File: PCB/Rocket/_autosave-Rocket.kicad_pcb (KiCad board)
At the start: 2 copper layers, 62.7 x 63.5 mm, 49 parts, among them J4 Micro_SD_Card, J5 Conn_ARM_JTAG_SWD_10, J7 1987724, U1 STM32L476RGTx, U2 MIC5365-3.3YC5-TR, U3 MC78L05ACDR2G

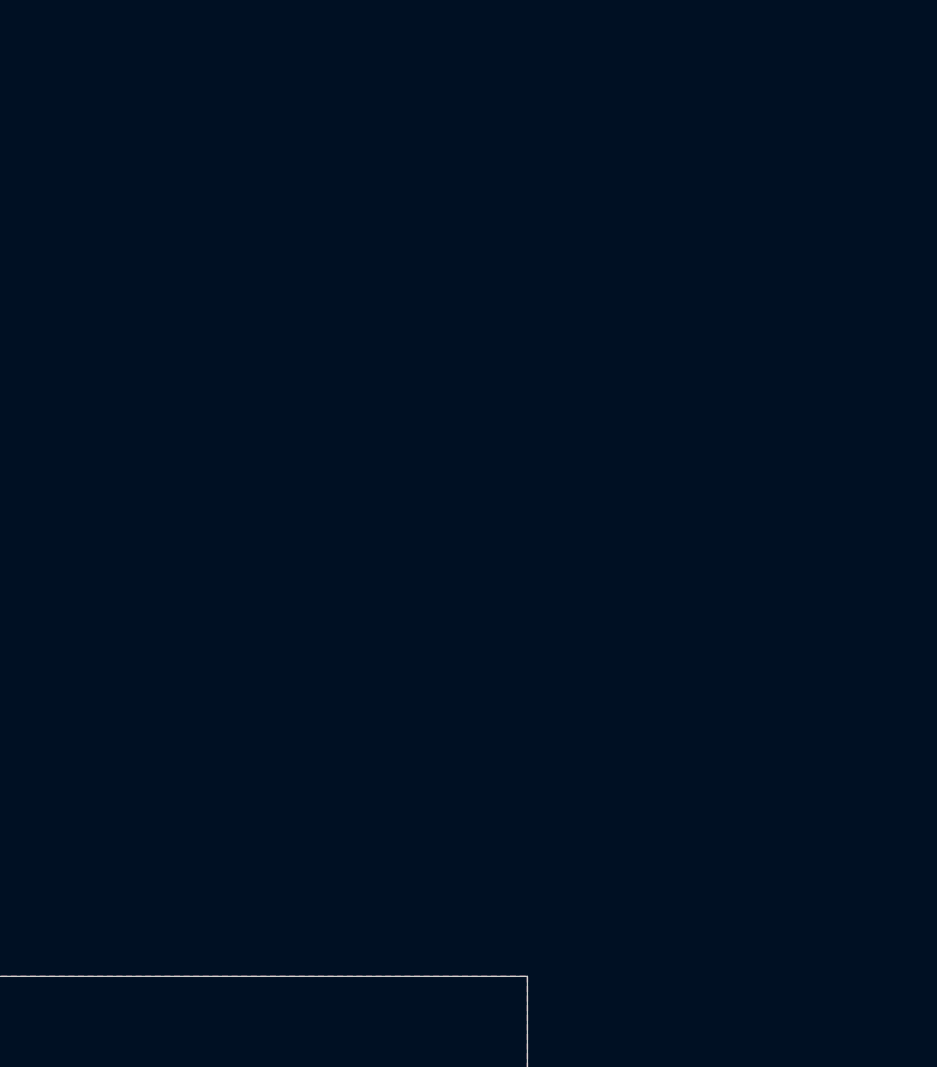
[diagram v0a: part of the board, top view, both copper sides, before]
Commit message: Updating to use arduino instead of STM32
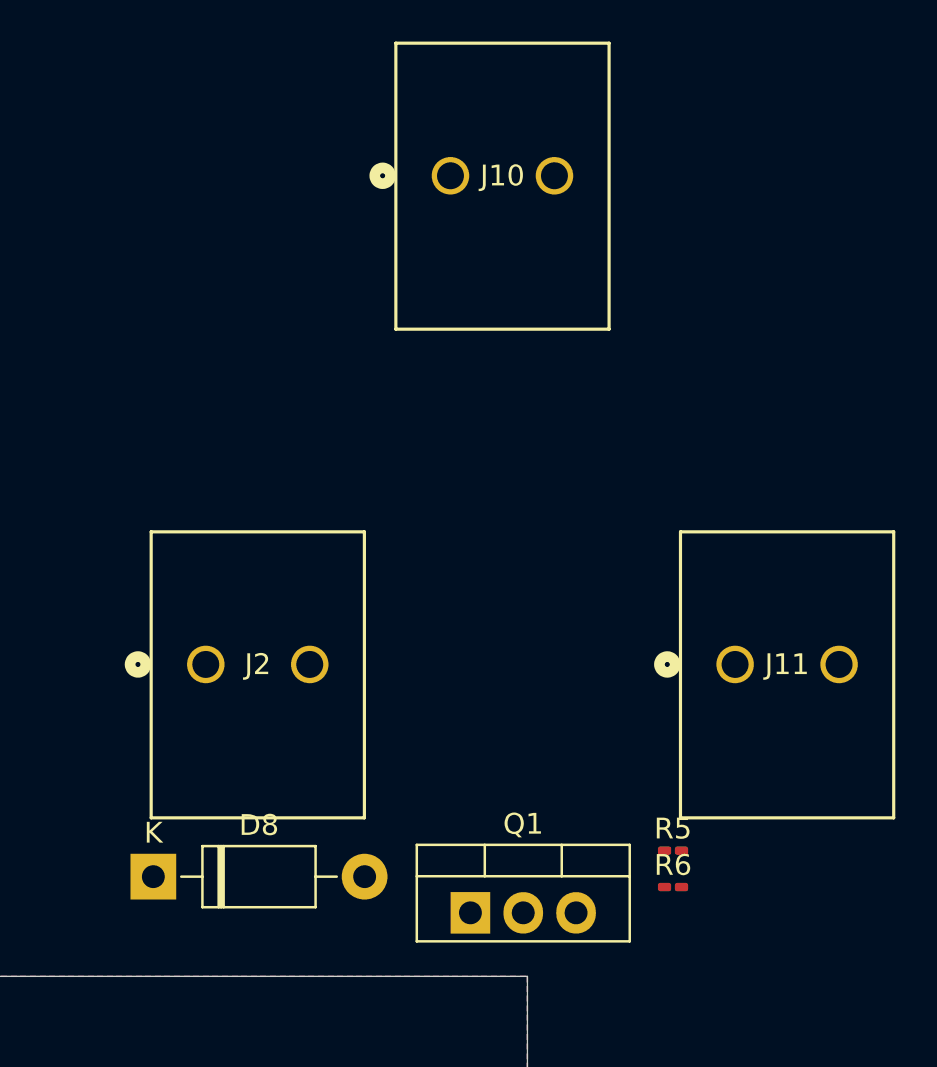
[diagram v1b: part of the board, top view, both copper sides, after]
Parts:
- added D8: 1N4001, Diode_THT:D_DO-41_SOD81_P10.16mm_Horizontal, F.Cu at (147.5, 32.0)
- added J10: 1987724, 1987724:CONN_1987724_PXC, F.Cu at (161.8, -1.70)
- added J11: 1987724, 1987724:CONN_1987724_PXC, F.Cu at (175.5, 21.8)
- added J2: 1987724, 1987724:CONN_1987724_PXC, F.Cu at (150.0, 21.8)
- added Q1: IRLZ44N, Package_TO_SOT_THT:TO-220-3_Vertical, F.Cu at (162.8, 33.7)
- added R5: 10k, Resistor_SMD:R_0201_0603Metric_Pad0.64x0.40mm_HandSolder, F.Cu at (172.5, 30.8)
- added R6: 220, Resistor_SMD:R_0201_0603Metric_Pad0.64x0.40mm_HandSolder, F.Cu at (172.5, 32.5)

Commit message: Updated PCB
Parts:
- U1: value STM32L476RGTx -> ATMEGA328P-PN; footprint Package_QFP:LQFP-64_10x10mm_P0.5mm -> Arduino:28P3_ATM
- moved U1 59.0 mm to (81.5, 53.5)
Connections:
- U1 pad 1: +3.3V -> unconnected-(U1-PC6-Pad1)
- U1 pad 12: GND -> unconnected-(U1-PD6-Pad12)
- U1 pad 13: +3.3VA -> /RX
- U1 pad 14: /PWM -> /TX
- U1 pad 15: /TACH -> unconnected-(U1-PB1-Pad15)
- U1 pad 16: /PRESSURE_OUT -> /CS
- U1 pad 17: unconnected-(U1-PA3-Pad17) -> /SCK
- U1 pad 18: GND -> /MISO
- U1 pad 19: +3.3V -> /MOSI
- U1 pad 20: /CS -> unconnected-(U1-AVCC-Pad20)
- U1 pad 21: /SCK -> unconnected-(U1-AREF-Pad21)
- U1 pad 22: /MISO -> unconnected-(U1-GND-Pad22)
- U1 pad 23: /MOSI -> /PWM
- U1 pad 27: unconnected-(U1-PB1-Pad27) -> /SDA
- U1 pad 28: unconnected-(U1-PB2-Pad28) -> /SCL
- U1 pad 5: /OSC_IN -> unconnected-(U1-PD3-Pad5)
- U1 pad 6: /OSC_OUT -> unconnected-(U1-PD4-Pad6)
- U1 pad 7: /NRST -> +5V
- U1 pad 8: unconnected-(U1-PC0-Pad8) -> GND
